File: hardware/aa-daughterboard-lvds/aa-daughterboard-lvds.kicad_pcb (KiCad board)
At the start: 4 copper layers, 145 parts, among them CN1 Barrel_Jack, CN10 6P6C, CN11 6P6C, CN12 6P6C, CN13 6P6C, CN14 Conn_01x08, CN15 Conn_01x08, CN16 Conn_01x08, CN17 8P8C, CN18 8P8C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

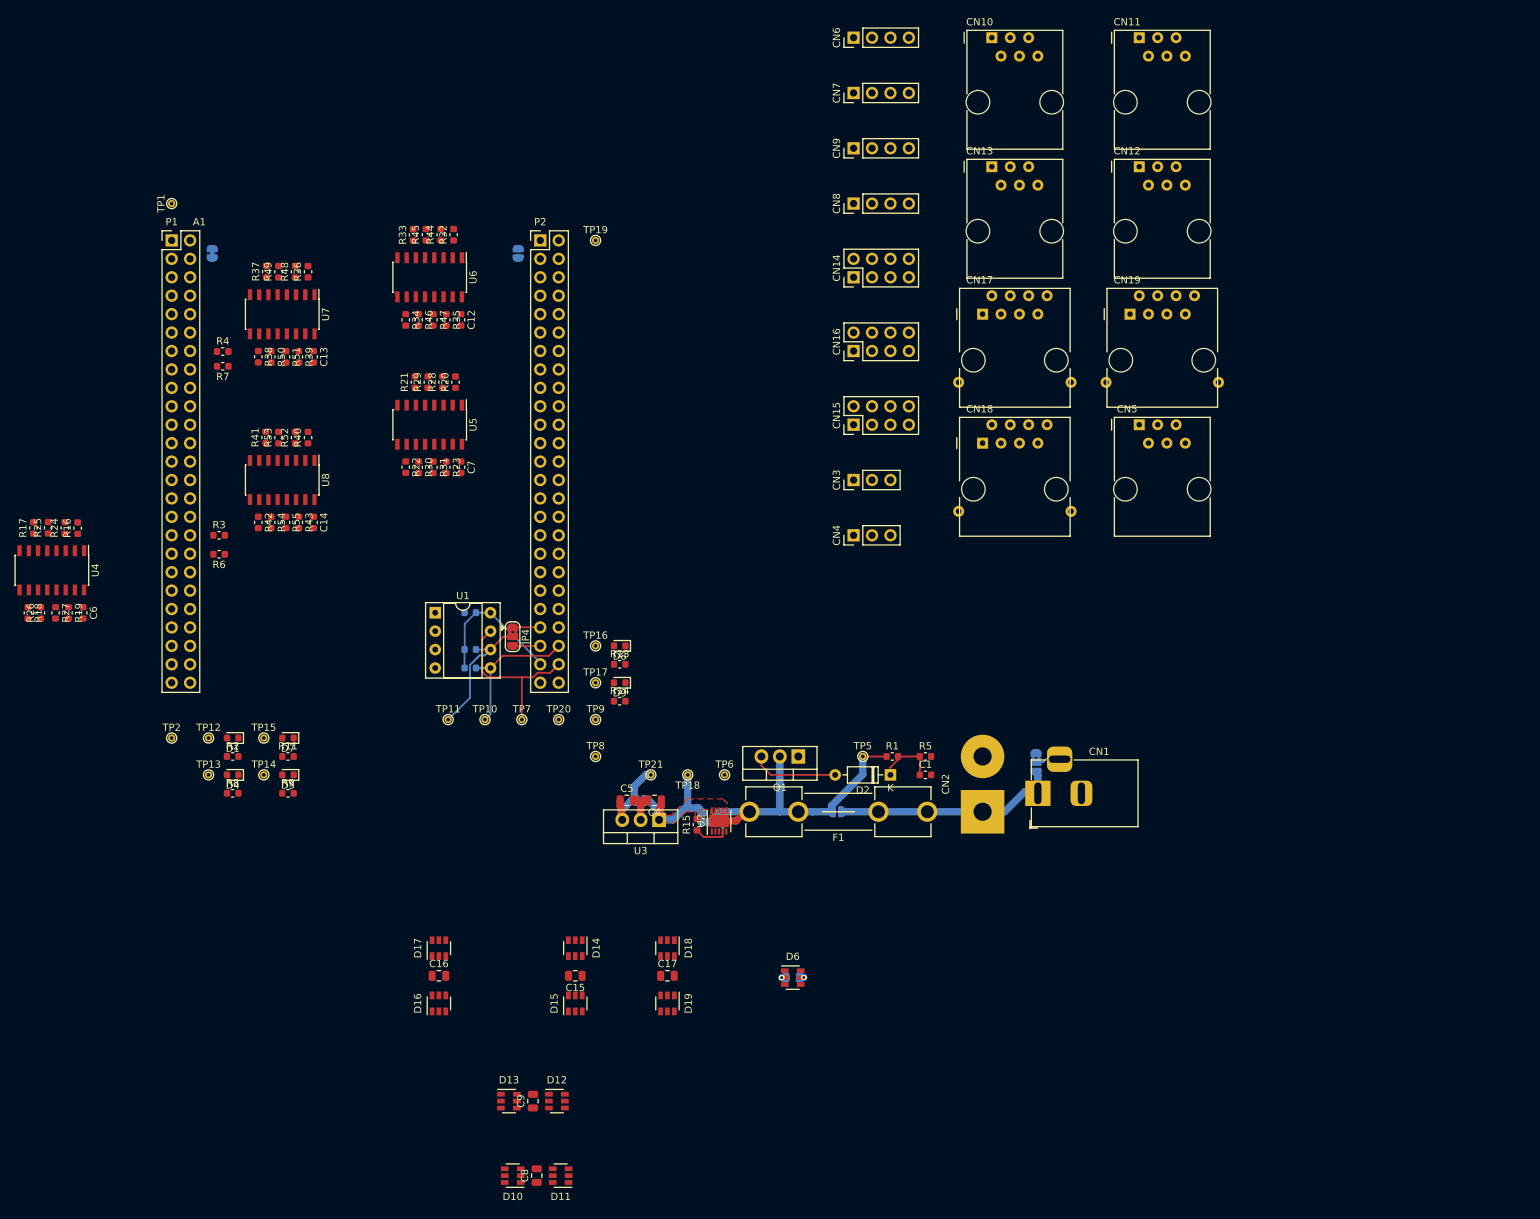
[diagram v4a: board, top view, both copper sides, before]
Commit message: Routed, labeling done pending double check
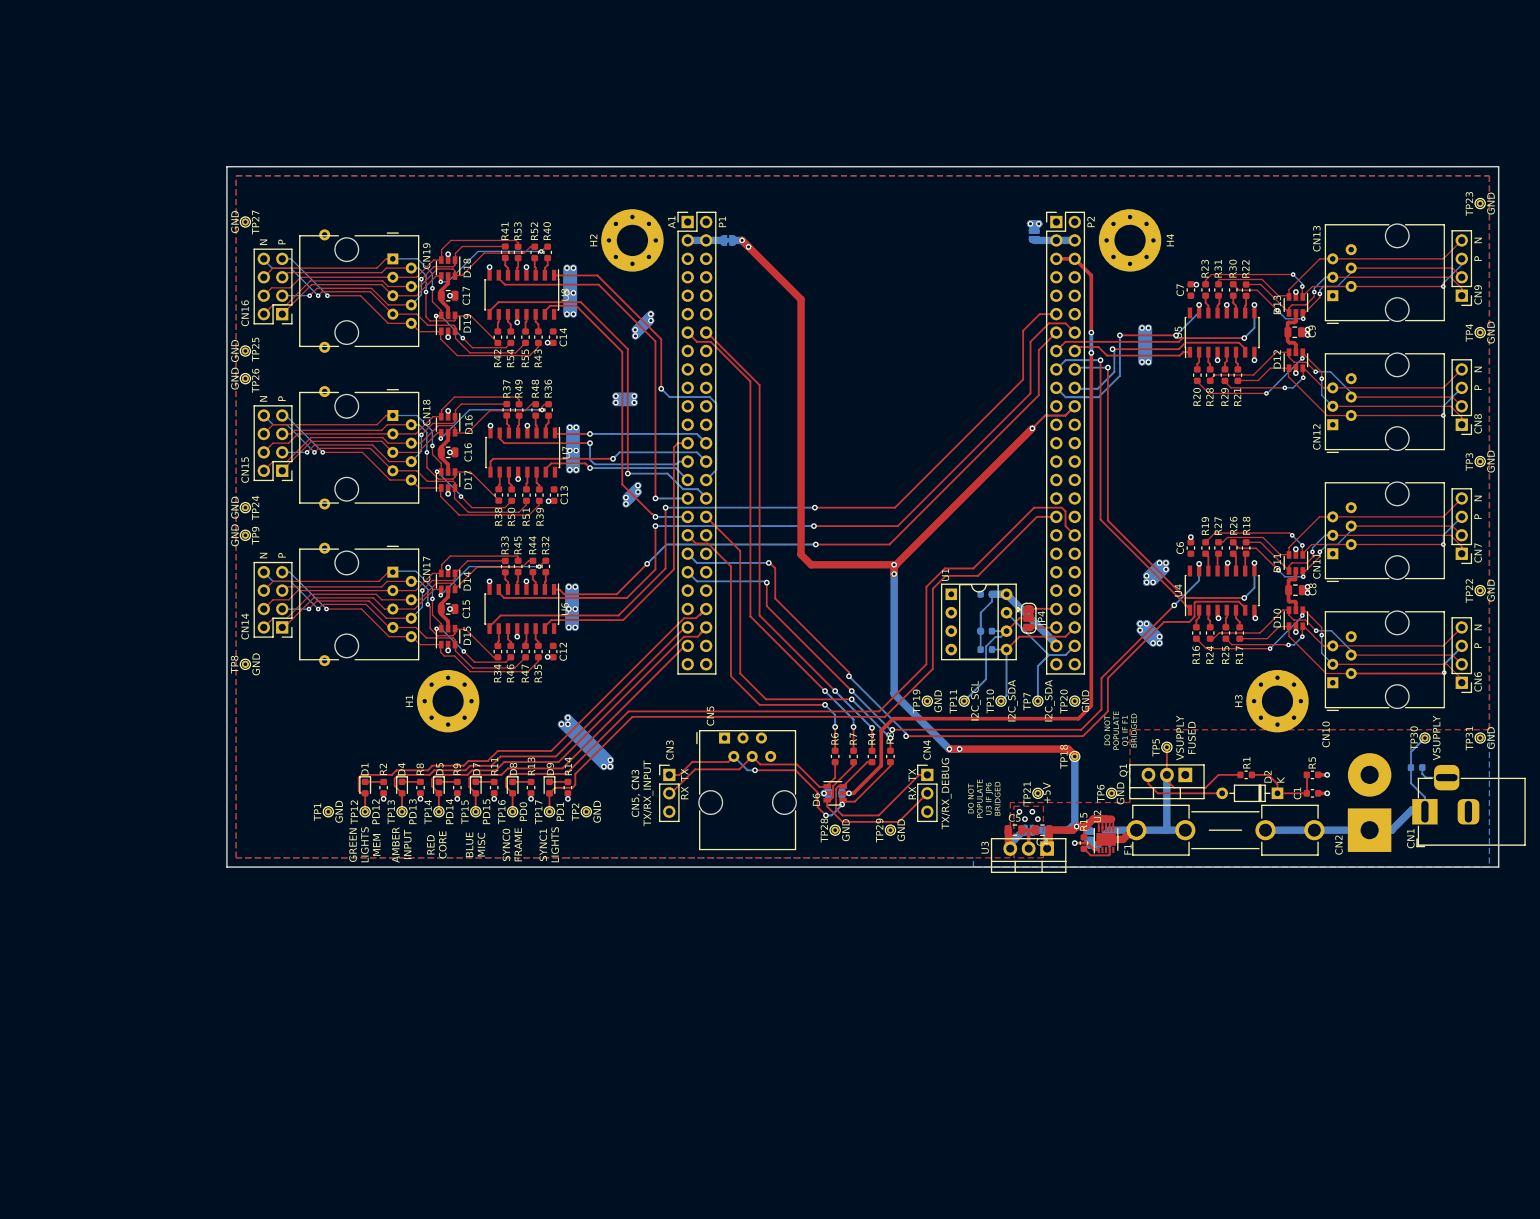
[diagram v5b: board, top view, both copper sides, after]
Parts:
- removed JP2: SolderJumper_3_Bridged12, Jumper:SolderJumper-3_P1.3mm_Bridged2Bar12_RoundedPad1.0x1.5mm
- removed JP3: SolderJumper_2_Open, Jumper:SolderJumper-2_P1.3mm_Open_RoundedPad1.0x1.5mm
- added H1: MountingHole_Pad, MountingHole:MountingHole_4.3mm_M4_Pad_Via, F.Cu at (83.8, 124.5)
- added H2: MountingHole_Pad, MountingHole:MountingHole_4.3mm_M4_Pad_Via, F.Cu at (109.2, 61.0)
- added H3: MountingHole_Pad, MountingHole:MountingHole_4.3mm_M4_Pad_Via, F.Cu at (198.1, 124.5)
- added H4: MountingHole_Pad, MountingHole:MountingHole_4.3mm_M4_Pad_Via, F.Cu at (177.8, 61.0)
- added R56: 10k, Resistor_SMD:R_0603_1608Metric, B.Cu at (217.3, 133.6)
- added TP22: TestPoint, TestPoint:TestPoint_THTPad_D1.0mm_Drill0.5mm, F.Cu at (226.1, 109.2)
- added TP23: TestPoint, TestPoint:TestPoint_THTPad_D1.0mm_Drill0.5mm, F.Cu at (226.1, 55.9)
- added TP24: TestPoint, TestPoint:TestPoint_THTPad_D1.0mm_Drill0.5mm, F.Cu at (55.9, 97.8)
- added TP25: TestPoint, TestPoint:TestPoint_THTPad_D1.0mm_Drill0.5mm, F.Cu at (55.9, 76.2)
- added TP26: TestPoint, TestPoint:TestPoint_THTPad_D1.0mm_Drill0.5mm, F.Cu at (55.9, 80.0)
- added TP27: TestPoint, TestPoint:TestPoint_THTPad_D1.0mm_Drill0.5mm, F.Cu at (55.9, 58.4)
- added TP28: TestPoint, TestPoint:TestPoint_THTPad_D1.0mm_Drill0.5mm, F.Cu at (137.2, 142.2)
- added TP29: TestPoint, TestPoint:TestPoint_THTPad_D1.0mm_Drill0.5mm, F.Cu at (144.8, 142.2)
- added TP3: TestPoint, TestPoint:TestPoint_THTPad_D1.0mm_Drill0.5mm, F.Cu at (226.1, 91.4)
- added TP30: TestPoint, TestPoint:TestPoint_THTPad_D1.0mm_Drill0.5mm, F.Cu at (218.4, 129.5)
- added TP31: TestPoint, TestPoint:TestPoint_THTPad_D1.0mm_Drill0.5mm, F.Cu at (226.1, 129.5)
- added TP4: TestPoint, TestPoint:TestPoint_THTPad_D1.0mm_Drill0.5mm, F.Cu at (226.1, 73.7)
- moved R18 168.1 mm to (193.8, 103.4), turned to 90 degrees
- moved R17 166.9 mm to (192.9, 115.1), turned to 270 degrees
- moved R26 164.6 mm to (192.0, 103.4)
- moved R25 163.0 mm to (191.0, 115.1), turned to 270 degrees
- moved U4 161.3 mm to (190.5, 109.2), turned to 90 degrees
- moved R27 160.5 mm to (190.0, 103.4), turned to 90 degrees
- moved R24 158.5 mm to (188.8, 115.1), turned to 270 degrees
- moved R19 157.0 mm to (188.2, 103.4), turned to 90 degrees
- moved R16 154.9 mm to (186.9, 115.1), turned to 270 degrees
- moved D13 154.3 mm to (200.7, 69.8), turned to 270 degrees
- moved C6 152.9 mm to (186.2, 103.4), turned to 90 degrees
- moved C9 149.2 mm to (200.5, 73.6), turned to 180 degrees
- moved D12 144.2 mm to (200.7, 77.5), turned to 90 degrees
- moved D10 132.5 mm to (200.7, 113.0), turned to 90 degrees
- moved C8 132.1 mm to (200.6, 109.2), turned to 180 degrees
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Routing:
- net VDD: track 17.8 -> 193.7 mm, vias 0 -> 8
- net +5V: track 11.0 -> 145.6 mm, vias 0 -> 54
- net /DB_SYNC_0: track 0.00 -> 108.0 mm
- net +3V: track 0.60 -> 108.0 mm, vias 1 -> 3
- net /TX_PANEL_2: track 0.00 -> 105.4 mm, vias 0 -> 2
- net /TX_PANEL_1: track 0.00 -> 104.0 mm, vias 0 -> 2
- net /PWM_CAP_1: track 0.00 -> 102.3 mm, vias 0 -> 3
- net /PWM_CAP_B: track 0.00 -> 95.7 mm, vias 0 -> 5
- net /DB_SYNC_1: track 0.00 -> 95.7 mm
- net /TX_PANEL_0: track 0.00 -> 88.2 mm, vias 0 -> 2
- net /RX_DEBUG: track 0.00 -> 68.2 mm, vias 0 -> 2
- net /TX_DEBUG: track 0.00 -> 67.2 mm, vias 0 -> 2
- net /DB_GREEN: track 0.00 -> 64.2 mm
- net /TX_STALK_B: track 0.00 -> 56.1 mm, vias 0 -> 3
- net /DB_ORANGE: track 0.00 -> 54.1 mm
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- added copper zone on F.Cu, net +5V
- added copper zone on B.Cu, net GND
- added copper zone on F.Cu, net GND
- removed copper zone on F.Cu, net VDD
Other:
- board outline added: 175.3 x 96.5 mm
- net class Default: clearance 0.2 -> 0.1524; trace_width 0.25 -> 0.254; via_dia 0.8 -> 0.7874; via_drill 0.4 -> 0.4064
- net class High Current: clearance 0.2 -> 0.1524; trace_width 1 -> 1.016; via_dia 0.8 -> 0.7874; via_drill 0.4 -> 0.4064
- net class Line Drive Broadside: clearance 0.2 -> 0.1524; trace_width 0.5 -> 0.508; via_dia 0.8 -> 0.7874; via_drill 0.4 -> 0.4064
- net class Line Drive Microstrip: clearance 0.2 -> 0.1524; trace_width 0.5 -> 0.1524; via_dia 0.8 -> 0.635; via_drill 0.4 -> 0.254
- net class Power: clearance 0.2 -> 0.1524; trace_width 1 -> 1.016; via_dia 0.8 -> 0.7874; via_drill 0.4 -> 0.4064
- rule trace_clearance: 0.2 -> 0.1524
- rule trace_min: 0.2 -> 0.1524
- rule via_min_drill: 0.3 -> 0.254
- rule via_min_size: 0.4 -> 0.381
- board text added: "+5V"
- board text added: "AMBER INPUT"
- board text added: "BLUE MISC"
- board text added: "BRIDGE JP5 IF U2 NOT POPULATED"
- board text added: "BRIDGE JP6 TO USE +5V FROM STM32F4 DISCOVERY BOARD A1 DO NOT POPULATE U3"
- board text added: "BRIDGE JP7 TO CONNECT VDD AND +5V POWER INPUT MUST BE REGULATED DO NOT POPULATE U3"
- board text added: "CN5, CN3 TX/RX_INPUT"
- board text added: "CUT JP1 IF STM32F4 DISCOVERY BOARD A1 IS INDEPENDENTLY POWERED"
- board text added: "DO NOT POPULATE Q1 IF F1 BRIDGED"
- board text added: "DO NOT POPULATE U3 IF JP6 BRIDGED"
- board text added: "GND"
- board text added: "GREEN LIGHTS MEM"
- board text added: "I2C_SCL"
- board text added: "I2C_SDA"
- board text added: "JP4 SELECTS I2C_SCL DEFAULT IS PA8 CUT 1-2, BRIDGE 2-3 TO SELECT PC8"
- board text added: "N"
- board text added: "P"
- board text added: "PD0"
- board text added: "PD1"
- board text added: "PD12"
- board text added: "PD13"
- board text added: "PD14"
- board text added: "PD15"
- board text added: "R56 CONNECTS VSUPPLY AND GND WHEN CN1 UNPLUGGED"
- board text added: "RED CORE"
- board text added: "RX"
- board text added: "SYNC0 FRAME"
- board text added: "SYNC1 LIGHTS"
- board text added: "TX"
- board text added: "TX/RX_DEBUG"
- board text added: "VSUPPLY"
- board text added: "VSUPPLY FUSED"

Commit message: Tweaks and labeling changes
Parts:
- moved C14 0.13 mm to (98.3, 74.4)
- moved C12 0.10 mm to (98.3, 117.7)
- moved C13 0.08 mm to (98.4, 96.1)
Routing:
- net +5V: track 145.6 -> 67.2 mm, vias 54 -> 8
- net /TX_STALK_B: track 56.1 -> 49.0 mm
- net /TX_INPUT: track 49.7 -> 45.4 mm
- net /RX_INPUT: track 44.2 -> 39.9 mm
- net /TX_PANEL_3: track 40.3 -> 38.4 mm, vias 0 -> 2
- net /TX_PANEL_1: track 104.0 -> 102.1 mm, vias 2 -> 4
- net /TX_STALK_A: track 33.5 -> 31.7 mm
- net /TX_STALK_1: track 46.1 -> 47.9 mm, vias 1 -> 3
- net /PWM_CAP_B: track 95.7 -> 93.9 mm
- net /TX_XP_2: track 52.0 -> 50.3 mm, vias 1 -> 3
- net /TX_STALK_2: track 16.7 -> 18.2 mm, vias 0 -> 2
- net /TX_XP_3: track 43.2 -> 41.7 mm, vias 1 -> 3
- net /TX_PANEL_5: track 29.8 -> 28.4 mm
- net /TX_PANEL_2: track 105.4 -> 104.2 mm, vias 2 -> 4
- net /PWM_CAP_2: track 29.1 -> 30.1 mm, vias 1 -> 3
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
